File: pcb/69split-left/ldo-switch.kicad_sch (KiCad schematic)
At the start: 4 parts, among them U2 TLV76133DCY

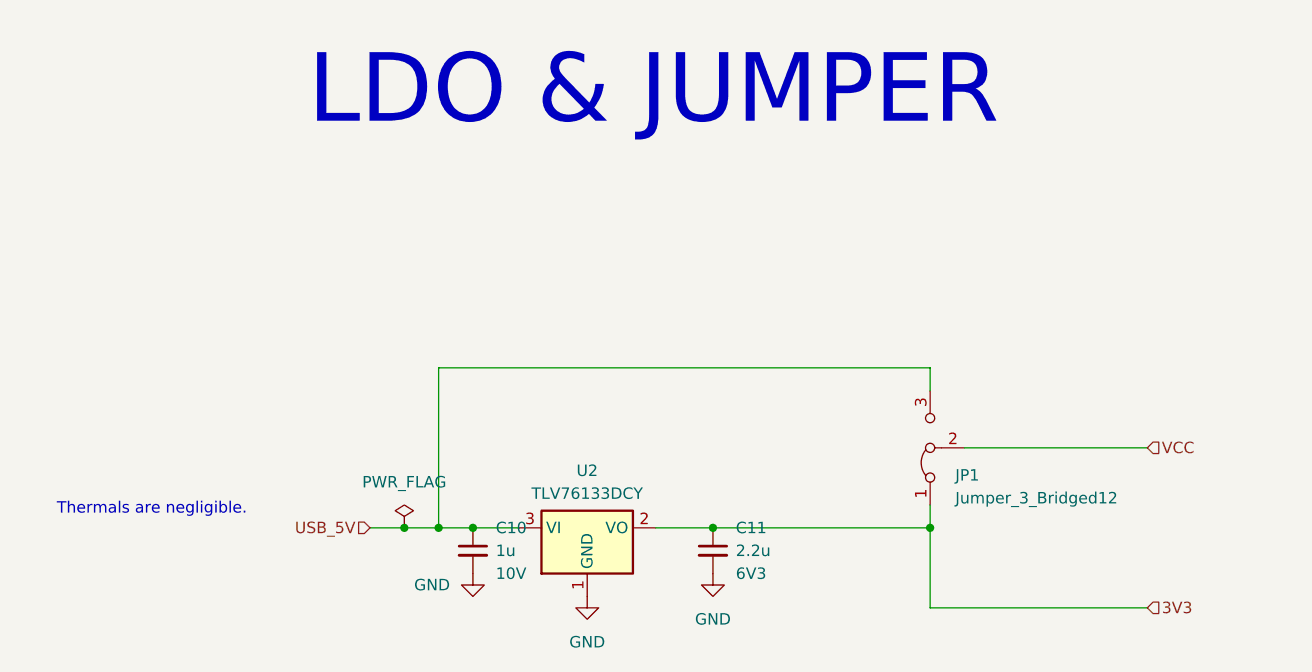
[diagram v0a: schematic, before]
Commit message: Added SPDT switch because I do not want to wait for the KiCAD librarians to approve of my SP3T switch, therefore that will be in future work.
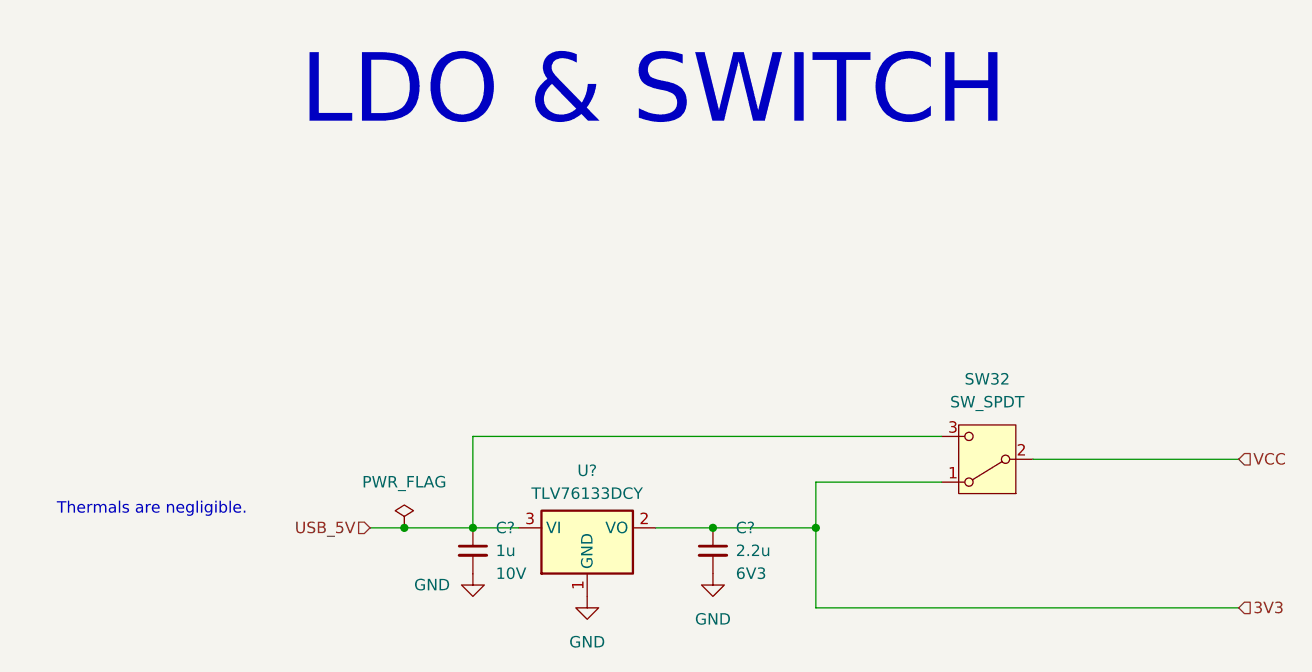
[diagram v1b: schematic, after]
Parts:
- removed JP1: Jumper_3_Bridged12, Connector_PinHeader_2.54mm:PinHeader_1x03_P2.54mm_Vertical, symbol Jumper:Jumper_3_Bridged12
- added SW32: SW_SPDT, Button_Switch_THT:SW_Slide_SPDT_Straight_CK_OS102011MS2Q, symbol Switch:SW_SPDT
- renumbered C10 to C?, C11 to C?, U2 to U?
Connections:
- net 3V3: now also SW32.1 (A)
- net USB_5V: now also SW32.3 (C)
- net VCC: now also SW32.2 (B)
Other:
- note added: "LDO & SWITCH"
- note removed: "LDO & JUMPER"
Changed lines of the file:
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@@
 		)
 	)
-	(text "LDO & JUMPER"
+	(text "LDO & SWITCH"
 		(exclude_from_sim no)
 		(at 103.886 27.686 0)
@@
 	)
 	(junction
-		(at 80.01 76.2)
-		(diameter 0)
-		(color 0 0 0 0)
-	)
-	(junction
 		(at 110.49 76.2)
 		(diameter 0)
@@
 	)
 	(junction
-		(at 134.62 76.2)
+		(at 121.92 76.2)
 		(diameter 0)
 		(color 0 0 0 0)
@@
 	(wire
 		(pts
-			(xy 134.62 73.66) (xy 134.62 76.2)
+			(xy 121.92 71.12) (xy 121.92 76.2)
+		)
+		(stroke
+			(width 0)
+			(type default)
+		)
+	)
+	(wire
+		(pts
+			(xy 121.92 71.12) (xy 135.89 71.12)
 		)
 		(stroke
@@
 	(wire
 		(pts
-			(xy 134.62 85.09) (xy 158.75 85.09)
-		)
-		(stroke
-			(width 0)
-			(type default)
-		)
-	)
-	(wire
-		(pts
-			(xy 80.01 76.2) (xy 83.82 76.2)
-		)
-		(stroke
-			(width 0)
-			(type default)
-		)
-	)
-	(wire
-		(pts
-			(xy 138.43 67.31) (xy 158.75 67.31)
-		)
-		(stroke
-			(width 0)
-			(type default)
-		)
-	)
-	(wire
-		(pts
-			(xy 110.49 76.2) (xy 134.62 76.2)
-		)
-		(stroke
-			(width 0)
-			(type default)
-		)
-	)
-	(wire
-		(pts
-			(xy 80.01 58.42) (xy 80.01 76.2)
+			(xy 121.92 85.09) (xy 168.91 85.09)
+		)
+		(stroke
+			(width 0)
+			(type default)
+		)
+	)
+	(wire
+		(pts
+			(xy 146.05 68.58) (xy 168.91 68.58)
+		)
+		(stroke
+			(width 0)
+			(type default)
+		)
+	)
+	(wire
+		(pts
+			(xy 110.49 76.2) (xy 121.92 76.2)
+		)
+		(stroke
+			(width 0)
+			(type default)
+		)
+	)
+	(wire
+		(pts
+			(xy 83.82 66.04) (xy 83.82 76.2)
 		)
 		(stroke
@@
 	(wire
 		(pts
-			(xy 80.01 58.42) (xy 134.62 58.42)
-		)
-		(stroke
-			(width 0)
-			(type default)
-		)
-	)
-	(wire
-		(pts
-			(xy 134.62 76.2) (xy 134.62 85.09)
-		)
-		(stroke
-			(width 0)
-			(type default)
-		)
-	)
-	(wire
-		(pts
-			(xy 134.62 58.42) (xy 134.62 60.96)
-		)
-		(stroke
-			(width 0)
-			(type default)
-		)
-	)
-	(wire
-		(pts
-			(xy 76.2 76.2) (xy 80.01 76.2)
+			(xy 83.82 66.04) (xy 135.89 66.04)
+		)
+		(stroke
+			(width 0)
+			(type default)
+		)
+	)
+	(wire
+		(pts
+			(xy 121.92 76.2) (xy 121.92 85.09)
+		)
+		(stroke
+			(width 0)
+			(type default)
+		)
+	)
+	(wire
+		(pts
+			(xy 76.2 76.2) (xy 83.82 76.2)
 		)
 		(stroke
@@
 	(hierarchical_label "3V3"
 		(shape input)
-		(at 158.75 85.09 0)
+		(at 168.91 85.09 0)
 		(effects
 			(font
@@
 	(hierarchical_label "VCC"
 		(shape input)
-		(at 158.75 67.31 0)
+		(at 168.91 68.58 0)
 		(effects
 			(font
@@
 		(dnp no)
 		(fields_autoplaced yes)
-		(property "Reference" "U2"
+		(property "Reference" "U?"
 			(at 96.52 69.85 0)
 			(effects
@@
 			(project "69split-left"
 				(path "/94301c1c-44b1-4926-ac38-8a25b84a2b23/cd421ade-5253-45fb-9a51-28ad04a50b20"
-					(reference "U2")
+					(reference "U?")
 					(unit 1)
 				)
@@
 		(dnp no)
 		(fields_autoplaced yes)
-		(property "Reference" "#PWR021"
+		(property "Reference" "#PWR?"
 			(at 83.82 87.63 0)
 			(effects
@@
 			(project "69split-left"
 				(path "/94301c1c-44b1-4926-ac38-8a25b84a2b23/cd421ade-5253-45fb-9a51-28ad04a50b20"
-					(reference "#PWR021")
+					(reference "#PWR?")
 					(unit 1)
 				)
@@
 		(dnp no)
 		(fields_autoplaced yes)
-		(property "Reference" "#PWR022"
+		(property "Reference" "#PWR?"
 			(at 110.49 87.63 0)
 			(effects
@@
 			(project "69split-left"
 				(path "/94301c1c-44b1-4926-ac38-8a25b84a2b23/cd421ade-5253-45fb-9a51-28ad04a50b20"
-					(reference "#PWR022")
+					(reference "#PWR?")
 					(unit 1)
 				)
@@
 		(dnp no)
 		(fields_autoplaced yes)
-		(property "Reference" "#PWR023"
+		(property "Reference" "#PWR?"
 			(at 96.52 90.17 0)
 			(effects
@@
 			(project "69split-left"
 				(path "/94301c1c-44b1-4926-ac38-8a25b84a2b23/cd421ade-5253-45fb-9a51-28ad04a50b20"
-					(reference "#PWR023")
+					(reference "#PWR?")
 					(unit 1)
 				)
@@
 		(dnp no)
 		(fields_autoplaced yes)
-		(property "Reference" "C10"
+		(property "Reference" "C?"
 			(at 86.36 76.2062 0)
 			(effects
@@
 			(project "69split-left"
 				(path "/94301c1c-44b1-4926-ac38-8a25b84a2b23/cd421ade-5253-45fb-9a51-28ad04a50b20"
-					(reference "C10")
-					(unit 1)
-				)
-			)
-		)
-	)
-	(symbol
-		(lib_id "Jumper:Jumper_3_Bridged12")
-		(at 134.62 67.31 90)
-		(unit 1)
-		(exclude_from_sim no)
-		(in_bom no)
-		(on_board yes)
-		(dnp no)
-		(property "Reference" "JP1"
-			(at 137.414 70.358 90)
-			(effects
-				(font
-					(size 1.27 1.27)
-				)
-				(justify right)
-			)
-		)
-		(property "Value" "Jumper_3_Bridged12"
-			(at 137.414 72.898 90)
-			(effects
-				(font
-					(size 1.27 1.27)
-				)
-				(justify right)
-			)
-		)
-		(property "Footprint" "Connector_PinHeader_2.54mm:PinHeader_1x03_P2.54mm_Vertical"
-			(at 134.62 67.31 0)
-			(effects
-				(font
-					(size 1.27 1.27)
-				)
-				(hide yes)
-			)
-		)
-		(property "Datasheet" "~"
-			(at 134.62 67.31 0)
-			(effects
-				(font
-					(size 1.27 1.27)
-				)
-				(hide yes)
-			)
-		)
-		(property "Description" "Jumper, 3-pole, pins 1+2 closed/bridged"
-			(at 134.62 67.31 0)
-			(effects
-				(font
-					(size 1.27 1.27)
-				)
-				(hide yes)
-			)
-		)
-		(property "Key" ""
-			(at 134.62 67.31 90)
-			(effects
-				(font
-					(size 1.27 1.27)
-				)
-				(hide yes)
-			)
-		)
-		(property "Untitled Field" ""
-			(at 134.62 67.31 90)
-			(effects
-				(font
-					(size 1.27 1.27)
-				)
-				(hide yes)
-			)
-		)
-		(property "MPN" "Generic"
-			(at 134.62 67.31 90)
-			(effects
-				(font
-					(size 1.27 1.27)
-				)
-				(hide yes)
-			)
-		)
-		(pin "1"
-		)
-		(pin "3"
-		)
-		(pin "2"
-		)
-		(instances
-			(project "69split"
-				(path "/1573ac28-80e2-4ab2-b20c-1c4896f37ece/800133d0-6e68-49ca-a870-e06397f7c02c/cd421ade-5253-45fb-9a51-28ad04a50b20"
-					(reference "JP?")
-					(unit 1)
-				)
-			)
-			(project "69split-left"
-				(path "/94301c1c-44b1-4926-ac38-8a25b84a2b23/cd421ade-5253-45fb-9a51-28ad04a50b20"
-					(reference "JP1")
+					(reference "C?")
 					(unit 1)
 				)
@@
 	)
 	(symbol
+		(lib_id "Switch:SW_SPDT")
+		(at 140.97 68.58 180)
+		(unit 1)
+		(exclude_from_sim no)
+		(in_bom yes)
+		(on_board yes)
+		(dnp no)
+		(fields_autoplaced yes)
+		(property "Reference" "SW32"
+			(at 140.97 59.69 0)
+			(effects
+				(font
+					(size 1.27 1.27)
+				)
+			)
+		)
+		(property "Value" "SW_SPDT"
+			(at 140.97 62.23 0)
+			(effects
+				(font
+					(size 1.27 1.27)
+				)
+			)
+		)
+		(property "Footprint" "Button_Switch_THT:SW_Slide_SPDT_Straight_CK_OS102011MS2Q"
+			(at 140.97 68.58 0)
+			(effects
+				(font
+					(size 1.27 1.27)
+				)
+				(hide yes)
+			)
+		)
+		(property "Datasheet" "~"
+			(at 140.97 60.96 0)
+			(effects
+				(font
+					(size 1.27 1.27)
+				)
+				(hide yes)
+			)
+		)
+		(property "Description" "Switch, single pole double throw"
+			(at 140.97 68.58 0)
+			(effects
+				(font
+					(size 1.27 1.27)
+				)
+				(hide yes)
+			)
+		)
+		(property "MPN" "OS102011MS2QN1"
+			(at 140.97 68.58 0)
+			(effects
+				(font
+					(size 1.27 1.27)
+				)
+				(hide yes)
+			)
+		)
+		(property "Rating" ""
+			(at 140.97 68.58 0)
+			(effects
+				(font
+					(size 1.27 1.27)
+				)
+				(hide yes)
+			)
+		)
+		(pin "1"
+		)
+		(pin "2"
+		)
+		(pin "3"
+		)
+		(instances
+			(project "69split-left"
+				(path "/94301c1c-44b1-4926-ac38-8a25b84a2b23/cd421ade-5253-45fb-9a51-28ad04a50b20"
+					(reference "SW32")
+					(unit 1)
+				)
+			)
+		)
+	)
+	(symbol
 		(lib_id "Device:C_Small")
 		(at 110.49 78.74 0)
@@
 		(dnp no)
 		(fields_autoplaced yes)
-		(property "Reference" "C11"
+		(property "Reference" "C?"
 			(at 113.03 76.2062 0)
 			(effects
@@
 			(project "69split-left"
 				(path "/94301c1c-44b1-4926-ac38-8a25b84a2b23/cd421ade-5253-45fb-9a51-28ad04a50b20"
-					(reference "C11")
-					(unit 1)
-				)
+					(reference "C?")
+					(unit 1)
+				)

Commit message: Final touches.
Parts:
- gave numbers to parts that had none: 3
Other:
- note added: "Thermals are negligible, unless you load the 3V3 pin so be careful with that."
- note removed: "Thermals are negligible."
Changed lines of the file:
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@@
 		(comment 2 "ymich9963")
 	)
-	(text "Thermals are negligible."
-		(exclude_from_sim no)
-		(at 37.592 74.168 0)
+	(text "Thermals are negligible,\nunless you load the 3V3 pin\nso be careful with that."
+		(exclude_from_sim no)
+		(at 33.274 76.2 0)
 		(effects
 			(font
@@
 	)
 	(hierarchical_label "3V3"
-		(shape input)
+		(shape output)
 		(at 168.91 85.09 0)
 		(effects
@@
 	)
 	(hierarchical_label "VCC"
-		(shape input)
+		(shape output)
 		(at 168.91 68.58 0)
 		(effects
@@
 		(dnp no)
 		(fields_autoplaced yes)
-		(property "Reference" "U?"
+		(property "Reference" "U2"
 			(at 96.52 69.85 0)
 			(effects
@@
 		)
 		(property "Key" ""
-			(at 96.52 76.2 0)
-			(effects
-				(font
-					(size 1.27 1.27)
-				)
-				(hide yes)
-			)
-		)
-		(property "Untitled Field" ""
 			(at 96.52 76.2 0)
 			(effects
@@
 			(project "69split-left"
 				(path "/94301c1c-44b1-4926-ac38-8a25b84a2b23/cd421ade-5253-45fb-9a51-28ad04a50b20"
-					(reference "U?")
+					(reference "U2")
 					(unit 1)
 				)
@@
 		(dnp no)
 		(fields_autoplaced yes)
-		(property "Reference" "#PWR?"
+		(property "Reference" "#PWR0101"
 			(at 83.82 87.63 0)
 			(effects
@@
 			(project "69split-left"
 				(path "/94301c1c-44b1-4926-ac38-8a25b84a2b23/cd421ade-5253-45fb-9a51-28ad04a50b20"
-					(reference "#PWR?")
+					(reference "#PWR0101")
 					(unit 1)
 				)
@@
 		(dnp no)
 		(fields_autoplaced yes)
-		(property "Reference" "#PWR?"
+		(property "Reference" "#PWR0103"
 			(at 110.49 87.63 0)
 			(effects
@@
 			(project "69split-left"
 				(path "/94301c1c-44b1-4926-ac38-8a25b84a2b23/cd421ade-5253-45fb-9a51-28ad04a50b20"
-					(reference "#PWR?")
+					(reference "#PWR0103")
 					(unit 1)
 				)
@@
 		(dnp no)
 		(fields_autoplaced yes)
-		(property "Reference" "#PWR?"
+		(property "Reference" "#PWR0102"
 			(at 96.52 90.17 0)
 			(effects
@@
 			(project "69split-left"
 				(path "/94301c1c-44b1-4926-ac38-8a25b84a2b23/cd421ade-5253-45fb-9a51-28ad04a50b20"
-					(reference "#PWR?")
+					(reference "#PWR0102")
 					(unit 1)
 				)
@@
 		(dnp no)
 		(fields_autoplaced yes)
-		(property "Reference" "C?"
+		(property "Reference" "C10"
 			(at 86.36 76.2062 0)
 			(effects
@@
 		)
 		(property "Key" ""
-			(at 83.82 78.74 0)
-			(effects
-				(font
-					(size 1.27 1.27)
-				)
-				(hide yes)
-			)
-		)
-		(property "Untitled Field" ""
 			(at 83.82 78.74 0)
 			(effects
@@
 			(project "69split-left"
 				(path "/94301c1c-44b1-4926-ac38-8a25b84a2b23/cd421ade-5253-45fb-9a51-28ad04a50b20"
-					(reference "C?")
+					(reference "C10")
 					(unit 1)
 				)
@@
 		(dnp no)
 		(fields_autoplaced yes)
-		(property "Reference" "C?"
+		(property "Reference" "C11"
 			(at 113.03 76.2062 0)
 			(effects
@@
 		)
 		(property "Key" ""
-			(at 110.49 78.74 0)
-			(effects
-				(font
-					(size 1.27 1.27)
-				)
-				(hide yes)
-			)
-		)
-		(property "Untitled Field" ""
 			(at 110.49 78.74 0)
 			(effects
@@
 			(project "69split-left"
 				(path "/94301c1c-44b1-4926-ac38-8a25b84a2b23/cd421ade-5253-45fb-9a51-28ad04a50b20"
-					(reference "C?")
-					(unit 1)
-				)
+					(reference "C11")
+					(unit 1)
+				)
